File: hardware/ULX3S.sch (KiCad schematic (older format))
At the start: 2 parts

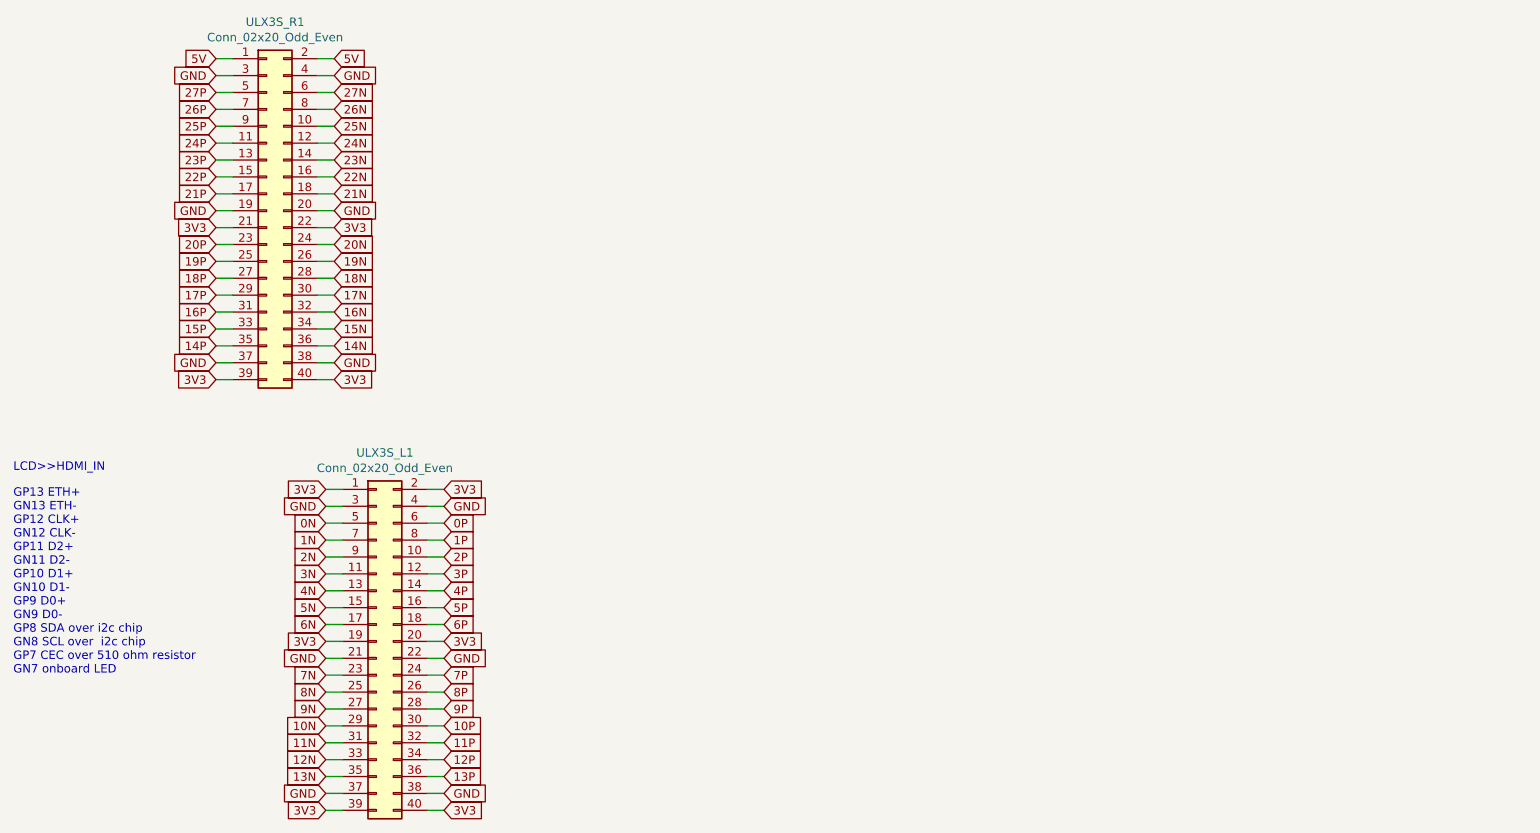
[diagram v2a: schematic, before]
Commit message: Adding ULX3S connections
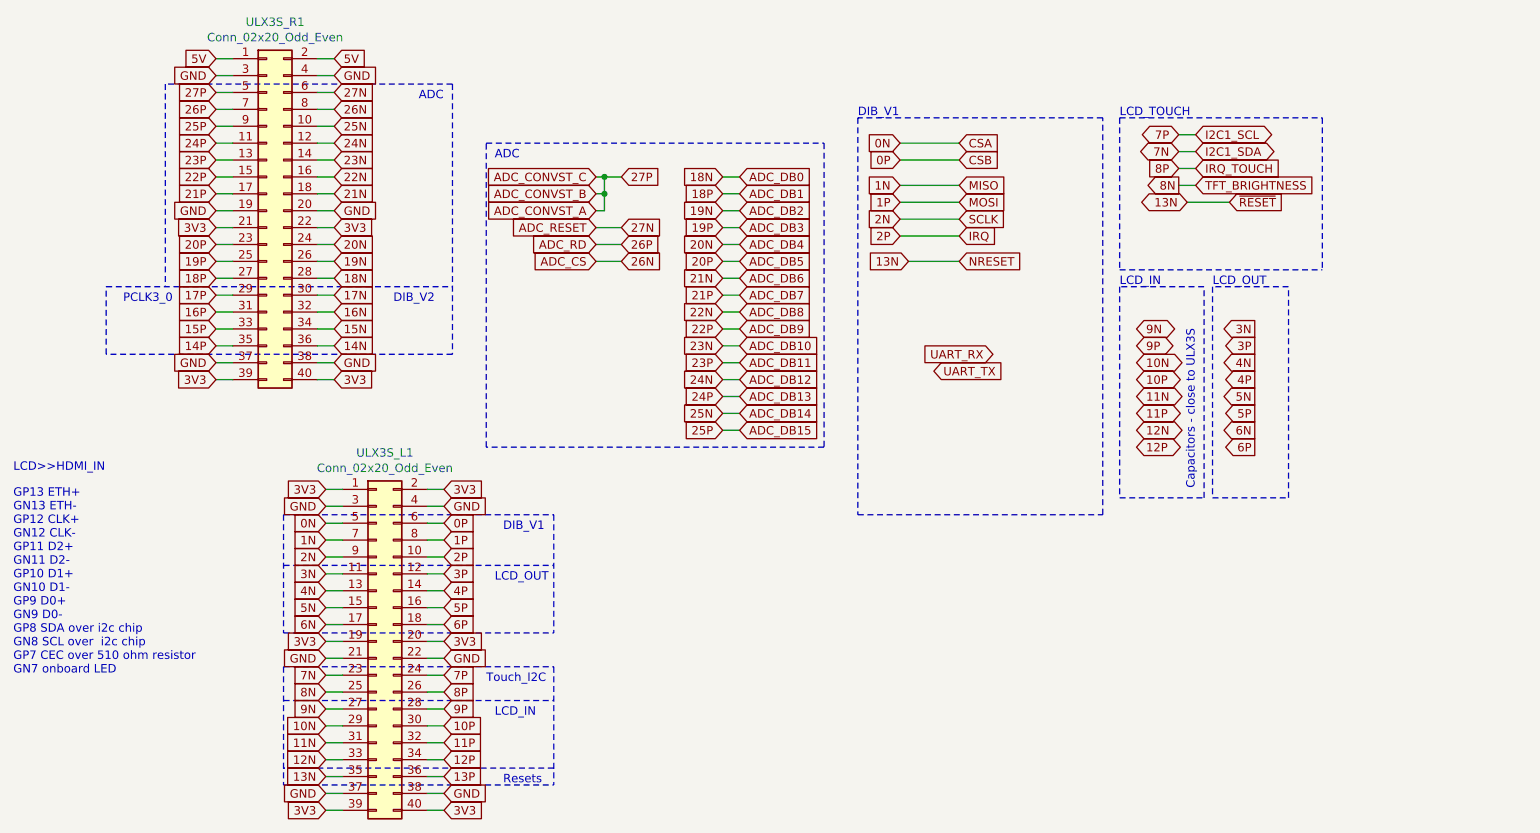
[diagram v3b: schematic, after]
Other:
- note added: "ADC"
- note added: "Capacitors - close to ULX3S"
- note added: "DIB_V1"
- note added: "DIB_V2"
- note added: "LCD_IN"
- note added: "LCD_OUT"
- note added: "LCD_TOUCH"
- note added: "PCLK3_0"
- note added: "Resets"
- note added: "Touch_I2C"

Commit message: Assigning footprints
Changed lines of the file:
@@
 Text GLabel 4200 2200 0    50   Input ~ 0
 ADC_CS
-Text GLabel 4950 2600 0    50   Input ~ 0
+Text GLabel 4950 2400 0    50   Input ~ 0
 22P
-Text GLabel 4950 2500 0    50   Input ~ 0
+Text GLabel 4950 2300 0    50   Input ~ 0
 22N
 Wire Wire Line
@@
 Text GLabel 4350 2200 2    50   Input ~ 0
 26N
+Text GLabel 4950 1800 0    50   Input ~ 0
+25P
+Text GLabel 4950 1700 0    50   Input ~ 0
+25N
+Text GLabel 4950 2000 0    50   Input ~ 0
+24P
+Text GLabel 4950 1900 0    50   Input ~ 0
+24N
+Text GLabel 4950 2200 0    50   Input ~ 0
+23P
+Text GLabel 4950 2100 0    50   Input ~ 0
+23N
+Text GLabel 4950 2600 0    50   Input ~ 0
+21P
+Text GLabel 4950 2500 0    50   Input ~ 0
+21N
+Text GLabel 4950 2800 0    50   Input ~ 0
+20P
+Text GLabel 4950 2700 0    50   Input ~ 0
+20N
+Text GLabel 4950 3000 0    50   Input ~ 0
+19P
+Text GLabel 4950 2900 0    50   Input ~ 0
+19N
 Text GLabel 4950 3200 0    50   Input ~ 0
-25P
+18P
 Text GLabel 4950 3100 0    50   Input ~ 0
-25N
-Text GLabel 4950 3000 0    50   Input ~ 0
-24P
-Text GLabel 4950 2900 0    50   Input ~ 0
-24N
-Text GLabel 4950 2800 0    50   Input ~ 0
-23P
-Text GLabel 4950 2700 0    50   Input ~ 0
-23N
-Text GLabel 4950 2400 0    50   Input ~ 0
-21P
-Text GLabel 4950 2300 0    50   Input ~ 0
-21N
-Text GLabel 4950 2200 0    50   Input ~ 0
-20P
-Text GLabel 4950 2100 0    50   Input ~ 0
-20N
-Text GLabel 4950 2000 0    50   Input ~ 0
-19P
-Text GLabel 4950 1900 0    50   Input ~ 0
-19N
-Text GLabel 4950 1800 0    50   Input ~ 0
-18P
-Text GLabel 4950 1700 0    50   Input ~ 0
 18N
 Text Notes 1400 2450 0    50   ~ 0

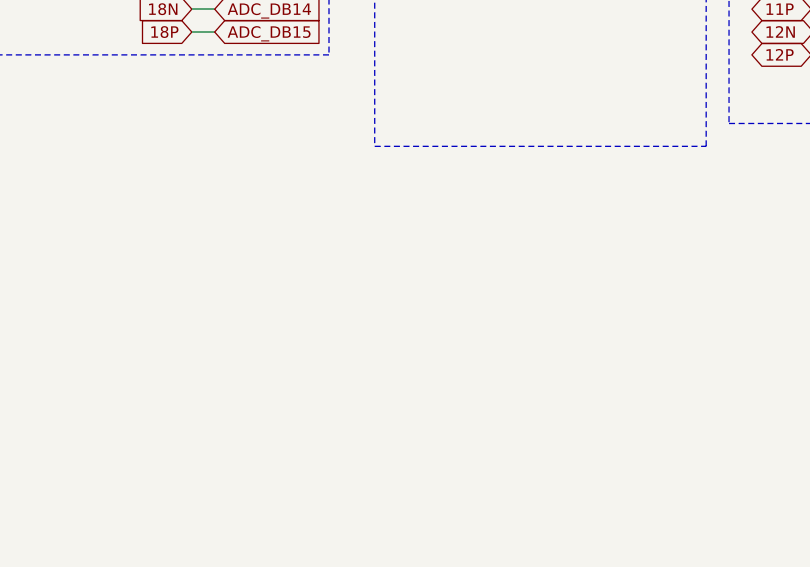
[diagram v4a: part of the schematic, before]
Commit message: Partially connecting ads8586s
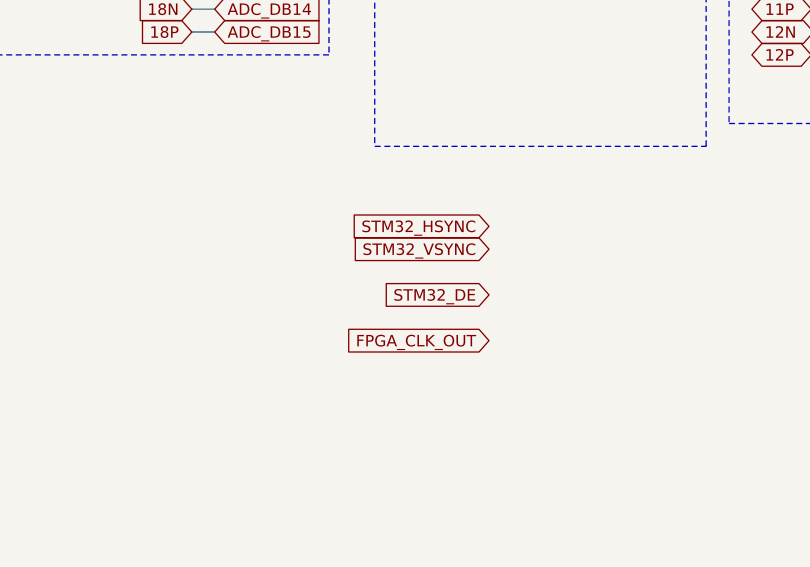
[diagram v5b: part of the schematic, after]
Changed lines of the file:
@@
 Text Notes 3000 2450 0    50   ~ 0
 DIB_V2
+Text GLabel 6250 4050 0    50   Input ~ 0
+STM32_HSYNC
+Text GLabel 6250 4150 0    50   Input ~ 0
+STM32_VSYNC
+Text GLabel 6250 4350 0    50   Input ~ 0
+STM32_DE
+Text GLabel 6250 4550 0    50   Input ~ 0
+FPGA_CLK_OUT
 $EndSCHEMATC

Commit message: Adding last known changes to shematics
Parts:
- added J?: VS_SCL, symbol Connector_Generic:Conn_01x03
- added J?: DE_IRQ, symbol Connector_Generic:Conn_01x03
- added J?: HS_SDA, symbol Connector_Generic:Conn_01x03
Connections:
- net 7N: now also J?.2 (Pin_2)
- net 7P: now also J?.2 (Pin_2)
- net 8P: now also J?.2 (Pin_2)
- net STM32_DE: now also J?.3 (Pin_3)
- net STM32_HSYNC: now also J?.3 (Pin_3)
- net STM32_VSYNC: now also J?.3 (Pin_3)
- new net I2C1_SCL: J?.1 (Pin_1)
- new net I2C1_SDA: J?.1 (Pin_1)
- new net IRQ_TOUCH: J?.1 (Pin_1)
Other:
- note added: "NRESET"
- note removed: "Resets"
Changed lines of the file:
@@
 $Descr A4 11693 8268
 encoding utf-8
-Sheet 3 11
+Sheet 3 10
 Title ""
-Date ""
-Rev ""
-Comp ""
+Date "2020-01-29"
+Rev "0.1"
+Comp "Envox d.o.o."
 Comment1 ""
 Comment2 ""
@@
 Text Notes 750  3450 0    50   ~ 0
 LCD>>HDMI_IN
-Text GLabel 6350 1750 2    50   Input ~ 0
+Text GLabel 6350 1600 2    50   Input ~ 0
 MISO
-Text GLabel 6350 1500 2    50   Input ~ 0
+Text GLabel 6350 1350 2    50   Input ~ 0
 CSA
-Text GLabel 6350 1600 2    50   Input ~ 0
+Text GLabel 6350 1450 2    50   Input ~ 0
 CSB
-Text GLabel 6350 1850 2    50   Input ~ 0
+Text GLabel 6350 1700 2    50   Input ~ 0
 MOSI
-Text GLabel 6350 1950 2    50   Input ~ 0
+Text GLabel 6350 1800 2    50   Input ~ 0
 SCLK
-Text GLabel 6350 2050 2    50   Input ~ 0
+Text GLabel 6350 1900 2    50   Input ~ 0
 IRQ
-Text GLabel 6350 2200 2    50   Input ~ 0
+Text GLabel 6350 2050 2    50   Input ~ 0
 NRESET
-Text GLabel 6550 2750 0    50   Input ~ 0
+Text GLabel 6250 2200 0    50   Input ~ 0
 UART_RX
-Text GLabel 6200 2850 2    50   Input ~ 0
+Text GLabel 5900 2300 2    50   Input ~ 0
 UART_TX
-Wire Notes Line
-	5750 3700 7200 3700
-Wire Notes Line
-	7200 3700 7200 1350
-Wire Notes Line
-	7200 1350 5750 1350
-Wire Notes Line
-	5750 1350 5750 3700
-Text Notes 5750 1350 0    50   ~ 0
+Text Notes 5750 1200 0    50   ~ 0
 DIB_V1
-Text GLabel 7650 1450 0    50   BiDi ~ 0
-7P
-Text GLabel 7650 1550 0    50   BiDi ~ 0
-7N
-Text GLabel 7750 1450 2    50   BiDi ~ 0
-I2C1_SCL
-Text GLabel 7750 1550 2    50   BiDi ~ 0
-I2C1_SDA
-Wire Wire Line
-	7650 1450 7750 1450
-Wire Wire Line
-	7650 1550 7750 1550
-Text GLabel 7650 1650 0    50   Input ~ 0
+Text GLabel 9200 1850 1    50   Input ~ 0
 8P
-Wire Wire Line
-	7650 1650 7750 1650
-Text GLabel 7650 1750 0    50   Output ~ 0
+Text GLabel 7550 2000 3    50   Output ~ 0
 8N
 Wire Wire Line
-	7650 1750 7750 1750
-Text GLabel 7950 1850 2    50   Input ~ 0
-~RESET
-Text GLabel 7750 1650 2    50   Input ~ 0
+	7550 2000 7550 1900
+Text GLabel 9300 1850 1    50   Input ~ 0
 IRQ_TOUCH
-Text GLabel 7750 1750 2    50   Input ~ 0
+Text GLabel 7550 1900 1    50   Input ~ 0
 TFT_BRIGHTNESS
-Text GLabel 7700 1850 0    50   BiDi ~ 0
+Text GLabel 4350 2400 2    50   BiDi ~ 0
 13N
-Wire Notes Line
-	7300 1350 8500 1350
-Wire Notes Line
-	8500 1350 8500 2250
-Wire Notes Line
-	7300 1350 7300 2250
-Wire Notes Line
-	7300 2250 8500 2250
-Text Notes 7300 1350 0    50   ~ 0
+Text Notes 7300 1200 0    50   ~ 0
 LCD_TOUCH
-Wire Wire Line
-	7950 1850 7700 1850
 Text GLabel 7400 3300 2    50   BiDi ~ 0
 12P
@@
 Text Notes 3650 3800 0    50   ~ 0
 DIB_V1
-Text GLabel 6000 1500 0    50   Input ~ 0
+Text GLabel 6000 1350 0    50   Input ~ 0
 0N
-Text GLabel 6000 1750 0    50   Input ~ 0
+Text GLabel 6000 1600 0    50   Input ~ 0
 1N
-Text GLabel 6000 1950 0    50   Input ~ 0
+Text GLabel 6000 1800 0    50   Input ~ 0
 2N
-Text GLabel 6000 1600 0    50   Input ~ 0
+Text GLabel 6000 1450 0    50   Input ~ 0
 0P
-Text GLabel 6000 1850 0    50   Input ~ 0
+Text GLabel 6000 1700 0    50   Input ~ 0
 1P
-Text GLabel 6000 2050 0    50   Input ~ 0
+Text GLabel 6000 1900 0    50   Input ~ 0
 2P
-Text GLabel 6050 2200 0    50   Input ~ 0
+Text GLabel 6050 2050 0    50   Input ~ 0
 13N
 Wire Wire Line
-	6000 1500 6350 1500
+	6000 1350 6350 1350
 Wire Wire Line
-	6000 1600 6350 1600
+	6000 1450 6350 1450
 Wire Wire Line
-	6000 1750 6350 1750
+	6000 1600 6350 1600
 Wire Wire Line
-	6000 1850 6350 1850
+	6000 1700 6350 1700
 Wire Wire Line
-	6000 1950 6350 1950
+	6000 1800 6350 1800
 Wire Wire Line
-	6050 2200 6350 2200
+	6050 2050 6350 2050
 Wire Wire Line
-	6000 2050 6350 2050
-Wire Notes Line
-	2350 5300 3950 5300
-Wire Notes Line
-	2350 4600 2350 5300
+	6000 1900 6350 1900
 Wire Notes Line
 	3950 4600 3950 5300
 Text Notes 3650 5300 0    50   ~ 0
-Resets
+NRESET
 Wire Wire Line
 	4950 1700 5050 1700
@@
 Text GLabel 4200 1800 0    50   Input ~ 0
 ADC_CONVST_B
-Text GLabel 4200 1700 0    50   Input ~ 0
-ADC_CONVST_C
 Text GLabel 4200 2100 0    50   Input ~ 0
 ADC_RD
@@
 22N
 Wire Wire Line
-	4200 1700 4250 1700
-Wire Wire Line
 	4200 1800 4250 1800
 Wire Wire Line
 	4250 1800 4250 1700
-Connection ~ 4250 1700
 Wire Wire Line
 	4250 1700 4350 1700
@@
 Text Notes 3000 2450 0    50   ~ 0
 DIB_V2
-Text GLabel 6250 4050 0    50   Input ~ 0
+Text GLabel 8450 1850 1    50   Input ~ 0
 STM32_HSYNC
-Text GLabel 6250 4150 0    50   Input ~ 0
+Text GLabel 7800 1850 1    50   Input ~ 0
 STM32_VSYNC
-Text GLabel 6250 4350 0    50   Input ~ 0
+Text GLabel 9100 1850 1    50   Input ~ 0
 STM32_DE
-Text GLabel 6250 4550 0    50   Input ~ 0
-FPGA_CLK_OUT
+Text GLabel 7450 1900 1    50   Input ~ 0
+ADC_BUSY
+Text GLabel 4200 2400 0    50   Input ~ 0
+ADC_FRSTDATA
+Wire Wire Line
+	4200 2400 4350 2400
+Wire Notes Line
+	2350 4600 2350 5200
+Wire Notes Line
+	3950 5300 2950 5300
+Wire Notes Line
+	2950 5300 2950 5200
+$Comp
+L Connector_Generic:Conn_01x03 J?
+U 1 1 5E7481BA
+P 7900 2150
+AR Path="/5E22D897/5E776450/5E7481BA" Ref="J?"  Part="1"
+AR Path="/5E22C01C/5E7481BA" Ref="J?"  Part="1"
+F 0 "J?" V 7773 2330 50  0000 L CNN
+F 1 "VS_SCL" V 7864 2330 50  0000 L CNN
+F 2 "" H 7900 2150 50  0001 C CNN
+F 3 "~" H 7900 2150 50  0001 C CNN
+	1    7900 2150
+	0    1    1    0
+$EndComp
+Text GLabel 8000 1850 1    50   BiDi ~ 0
+I2C1_SCL
+Text GLabel 7900 1850 1    50   BiDi ~ 0
+7P
+$Comp
+L Connector_Generic:Conn_01x03 J?
+U 1 1 5E7548B6
+P 9200 2150
+AR Path="/5E22D897/5E776450/5E7548B6" Ref="J?"  Part="1"
+AR Path="/5E22C01C/5E7548B6" Ref="J?"  Part="1"
+F 0 "J?" V 9073 2330 50  0000 L CNN
+F 1 "DE_IRQ" V 9164 2330 50  0000 L CNN
+F 2 "" H 9200 2150 50  0001 C CNN
+F 3 "~" H 9200 2150 50  0001 C CNN
+	1    9200 2150
+	0    1    1    0
+$EndComp
+Text GLabel 8650 1850 1    50   BiDi ~ 0
+I2C1_SDA
+Text GLabel 8550 1850 1    50   BiDi ~ 0
+7N
+$Comp
+L Connector_Generic:Conn_01x03 J?
+U 1 1 5E772205
+P 8550 2150
+AR Path="/5E22D897/5E776450/5E772205" Ref="J?"  Part="1"
+AR Path="/5E22C01C/5E772205" Ref="J?"  Part="1"
+F 0 "J?" V 8423 2330 50  0000 L CNN
+F 1 "HS_SDA" V 8514 2330 50  0000 L CNN
+F 2 "" H 8550 2150 50  0001 C CNN
+F 3 "~" H 8550 2150 50  0001 C CNN
+	1    8550 2150
+	0    1    1    0
+$EndComp
+Text GLabel 7450 2000 3    50   Input ~ 0
+17N
+Wire Wire Line
+	7450 2000 7450 1900
+Wire Wire Line
+	9300 1850 9300 1950
+Wire Wire Line
+	9200 1850 9200 1950
+Wire Wire Line
+	9100 1850 9100 1950
+Wire Wire Line
+	8650 1850 8650 1950
+Wire Wire Line
+	8550 1850 8550 1950
+Wire Wire Line
+	8450 1850 8450 1950
+Wire Wire Line
+	8000 1850 8000 1950
+Wire Wire Line
+	7900 1850 7900 1950
+Wire Wire Line
+	7800 1850 7800 1950
+Wire Notes Line
+	7300 1200 9700 1200
+Wire Notes Line
+	9700 1200 9700 2250
+Wire Notes Line
+	7300 1200 7300 2250
+Wire Notes Line
+	7300 2250 9700 2250
+Wire Notes Line
+	5750 1200 5750 2400
+Wire Notes Line
+	5750 1200 6750 1200
+Wire Notes Line
+	6750 1200 6750 2400
+Wire Notes Line
+	6750 2400 5750 2400
 $EndSCHEMATC

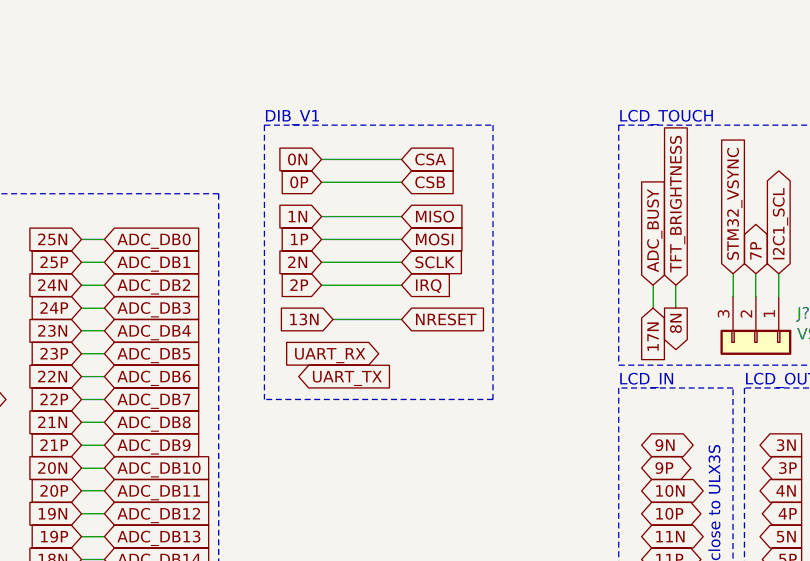
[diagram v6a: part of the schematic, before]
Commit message: Renaming wires
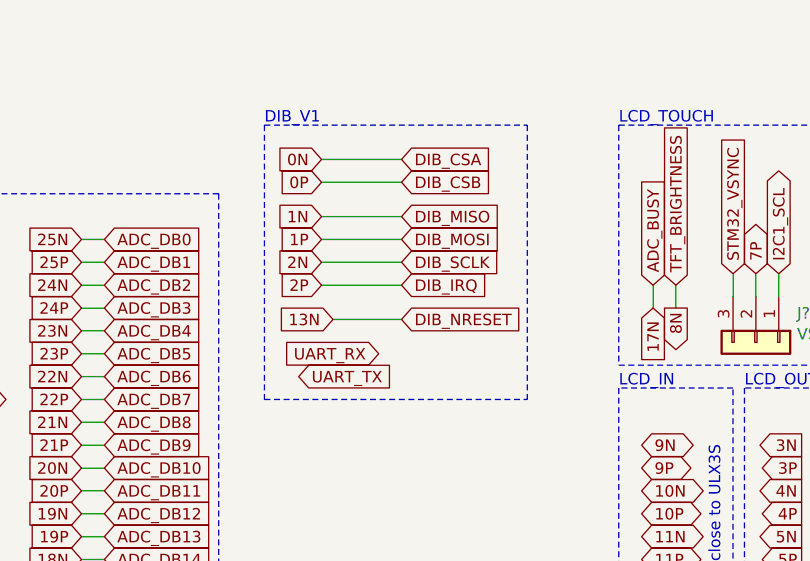
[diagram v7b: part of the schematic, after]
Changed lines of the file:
@@
 LCD>>HDMI_IN
 Text GLabel 6350 1600 2    50   Input ~ 0
-MISO
+DIB_MISO
 Text GLabel 6350 1350 2    50   Input ~ 0
-CSA
+DIB_CSA
 Text GLabel 6350 1450 2    50   Input ~ 0
-CSB
+DIB_CSB
 Text GLabel 6350 1700 2    50   Input ~ 0
-MOSI
+DIB_MOSI
 Text GLabel 6350 1800 2    50   Input ~ 0
-SCLK
+DIB_SCLK
 Text GLabel 6350 1900 2    50   Input ~ 0
-IRQ
+DIB_IRQ
 Text GLabel 6350 2050 2    50   Input ~ 0
-NRESET
+DIB_NRESET
 Text GLabel 6250 2200 0    50   Input ~ 0
 UART_RX
@@
 	5750 1200 5750 2400
 Wire Notes Line
-	5750 1200 6750 1200
-Wire Notes Line
-	6750 1200 6750 2400
-Wire Notes Line
-	6750 2400 5750 2400
+	6900 1200 6900 2400
+Wire Notes Line
+	5750 1200 6900 1200
+Wire Notes Line
+	5750 2400 6900 2400
 $EndSCHEMATC

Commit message: Routing board
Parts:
- J2, J6, J8: renamed from J?; footprint (none) -> Connector_PinHeader_2.00mm:PinHeader_1x03_P2.00mm_Vertical
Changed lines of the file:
@@
 P 7900 2150
 AR Path="/5E22D897/5E776450/5E7481BA" Ref="J?"  Part="1"
-AR Path="/5E22C01C/5E7481BA" Ref="J?"  Part="1"
-F 0 "J?" V 7773 2330 50  0000 L CNN
+AR Path="/5E22C01C/5E7481BA" Ref="J2"  Part="1"
+F 0 "J2" V 7773 2330 50  0000 L CNN
 F 1 "VS_SCL" V 7864 2330 50  0000 L CNN
-F 2 "" H 7900 2150 50  0001 C CNN
+F 2 "Connector_PinHeader_2.00mm:PinHeader_1x03_P2.00mm_Vertical" H 7900 2150 50  0001 C CNN
 F 3 "~" H 7900 2150 50  0001 C CNN
 	1    7900 2150
@@
 P 9200 2150
 AR Path="/5E22D897/5E776450/5E7548B6" Ref="J?"  Part="1"
-AR Path="/5E22C01C/5E7548B6" Ref="J?"  Part="1"
-F 0 "J?" V 9073 2330 50  0000 L CNN
+AR Path="/5E22C01C/5E7548B6" Ref="J8"  Part="1"
+F 0 "J8" V 9073 2330 50  0000 L CNN
 F 1 "DE_IRQ" V 9164 2330 50  0000 L CNN
-F 2 "" H 9200 2150 50  0001 C CNN
+F 2 "Connector_PinHeader_2.00mm:PinHeader_1x03_P2.00mm_Vertical" H 9200 2150 50  0001 C CNN
 F 3 "~" H 9200 2150 50  0001 C CNN
 	1    9200 2150
@@
 P 8550 2150
 AR Path="/5E22D897/5E776450/5E772205" Ref="J?"  Part="1"
-AR Path="/5E22C01C/5E772205" Ref="J?"  Part="1"
-F 0 "J?" V 8423 2330 50  0000 L CNN
+AR Path="/5E22C01C/5E772205" Ref="J6"  Part="1"
+F 0 "J6" V 8423 2330 50  0000 L CNN
 F 1 "HS_SDA" V 8514 2330 50  0000 L CNN
-F 2 "" H 8550 2150 50  0001 C CNN
+F 2 "Connector_PinHeader_2.00mm:PinHeader_1x03_P2.00mm_Vertical" H 8550 2150 50  0001 C CNN
 F 3 "~" H 8550 2150 50  0001 C CNN
 	1    8550 2150
@@
 Wire Notes Line
 	5750 2400 6900 2400
+$Comp
+L EEZ_DIB_MCU_r1B1-eagle-import:GND #SUPPLY0113
+U 1 1 5E3FFA5A
+P 4200 3800
+F 0 "#SUPPLY0113" H 4200 3800 50  0001 C CNN
+F 1 "GND" H 4200 3670 59  0000 C CNN
+F 2 "" H 4200 3800 50  0001 C CNN
+F 3 "" H 4200 3800 50  0001 C CNN
+	1    4200 3800
+	1    0    0    -1
+$EndComp
+Text GLabel 4200 3600 1    50   Input ~ 0
+GND
+Wire Wire Line
+	4200 3600 4200 3700
 $EndSCHEMATC
